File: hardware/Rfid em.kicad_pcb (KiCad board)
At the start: 2 copper layers, 92.7 x 65.1 mm, 18 parts, among them IC1 EM4095, J1 Conn_01x06, U1 560uH, U2 AMS1117-5.0

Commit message: fix: Add 10µF input capacitor for AMS1117-5.0
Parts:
- added C8: 10 uF, Capacitor_SMD:C_0805_2012Metric, F.Cu at (120.3, 90.5)
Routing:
- net Net-(J1-Pin_1): track 36.7 -> 50.2 mm, vias 1 -> 2
- net GND: track 86.3 -> 91.7 mm

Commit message: fix: Specify capacitor parts and place decoupling caps per datasheets
Use tantalum capacitors with MPNs for the AMS1117-5.0 (10µF input, 22µF output) and add a 100nF decoupling capacitor for the EM4095. Place C8 at U2 VIN, C1 at the U2 VOUT tab and C9 across IC1 DVDD/DVSS, link the footprints to their schematic symbols and move C9 into the schematic frame.
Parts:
- added C9: 100 nF, Capacitor_SMD:C_0805_2012Metric, F.Cu at (123.3, 83.2)
- C1: value 100 nF -> 22 uF; footprint Capacitor_SMD:C_0805_2012Metric -> Capacitor_Tantalum_SMD:CP_EIA-3528-21_Kemet-B
- C8: footprint Capacitor_SMD:C_0805_2012Metric -> Capacitor_Tantalum_SMD:CP_EIA-3216-18_Kemet-A
- moved C1 18.6 mm to (124.1, 95.5), turned to 90 degrees
- moved C8 12.1 mm to (113.7, 100.6), turned to 0 degrees
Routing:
- net GND: track 91.7 -> 106.3 mm, vias 2 -> 4
- net Net-(J1-Pin_1): track 50.2 -> 39.5 mm, vias 2 -> 1
- net VDD: track 43.9 -> 47.0 mm, vias 0 -> 2

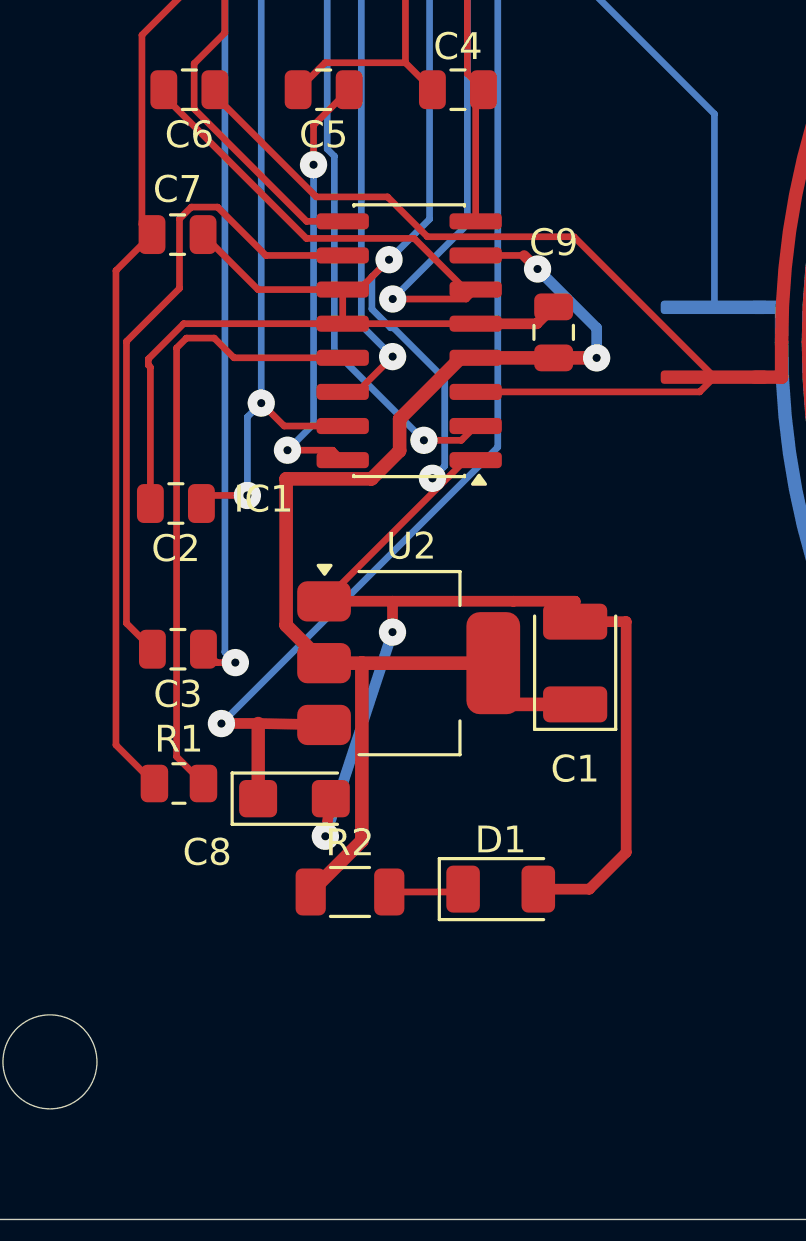
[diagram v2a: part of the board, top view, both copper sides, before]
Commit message: fix: Add MPNs, generate BOM from schematic and improve decoupling
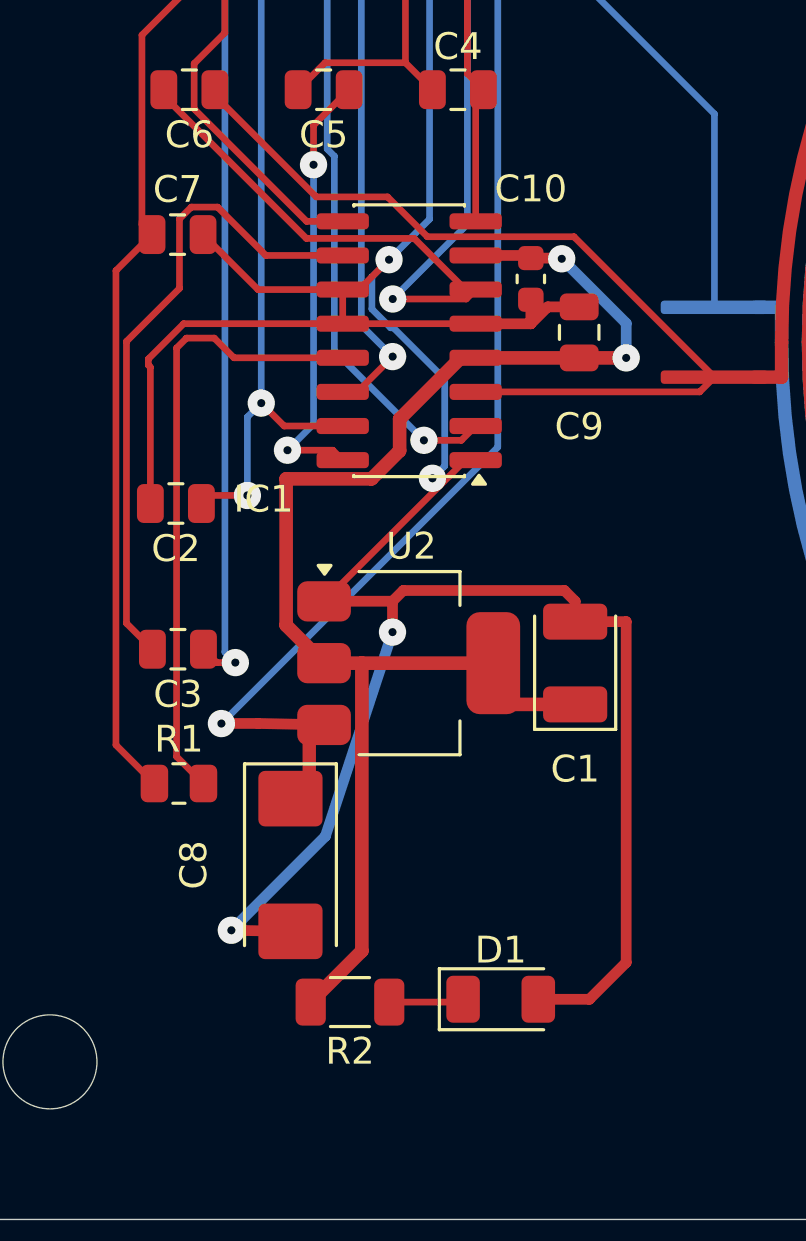
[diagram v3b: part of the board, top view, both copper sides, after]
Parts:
- added C10: 100 nF, Capacitor_SMD:C_0603_1608Metric, F.Cu at (122.5, 81.2)
- C8: footprint Capacitor_Tantalum_SMD:CP_EIA-3216-18_Kemet-A -> Capacitor_Tantalum_SMD:CP_EIA-6032-28_Kemet-C
- moved D1 4.10 mm to (121.3, 108.1)
- moved R2 4.10 mm to (115.7, 108.2)
- moved C8 2.47 mm to (113.5, 103.1), turned to -90 degrees
- moved C9 0.95 mm to (124.2, 83.2)
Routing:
- net GND: track 106.3 -> 118.3 mm
- net VDD: track 47.0 -> 53.3 mm
